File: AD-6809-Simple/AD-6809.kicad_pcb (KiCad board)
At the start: 2 copper layers, 100 x 100 mm, 41 parts, among them J1 SERIAL, J2 GAMECLK, J3 BARREL_JACK, J4 BAUD, J5 NMI, J6 RESET, SW1 RESET, U1 28C64, U2 6809, U3 28C64/IMS1630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

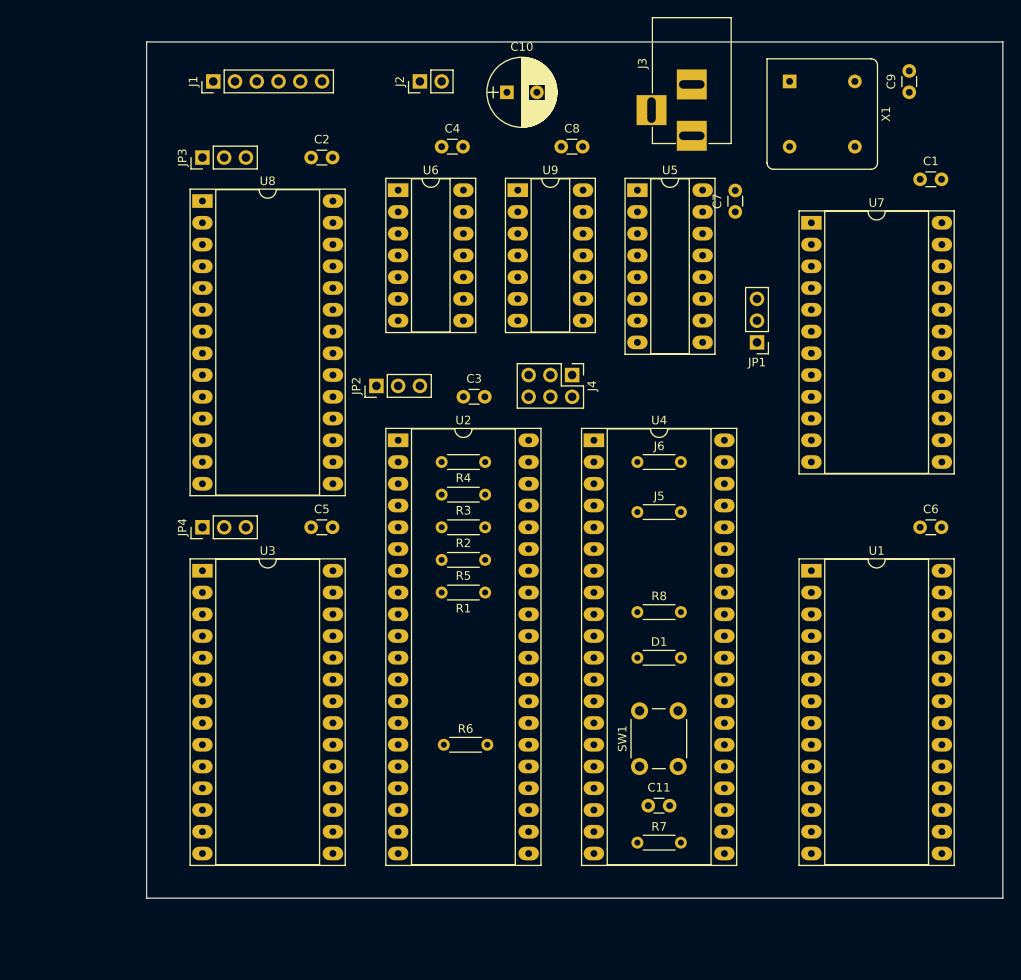
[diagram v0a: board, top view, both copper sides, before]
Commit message: Padded out the test programs to be rom sized.
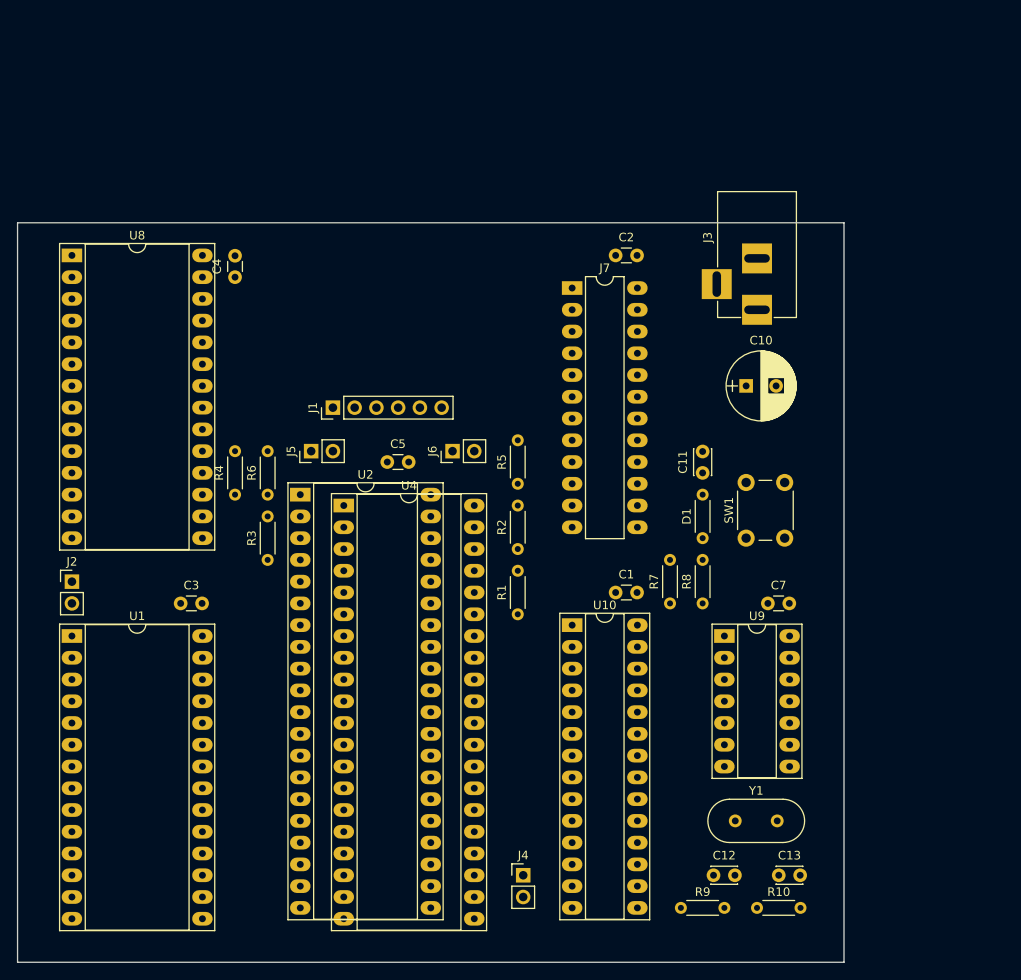
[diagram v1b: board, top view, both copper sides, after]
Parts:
- removed C6, C8, C9: 0.1uF, Capacitors_ThroughHole:C_Disc_D3.0mm_W1.6mm_P2.50mm
- removed JP1: Disable, Socket_Strips:Socket_Strip_Straight_1x03_Pitch2.54mm
- removed JP2: CLKSRC, Socket_Strips:Socket_Strip_Straight_1x03_Pitch2.54mm
- removed JP3, JP4: ROM RAM, Socket_Strips:Socket_Strip_Straight_1x03_Pitch2.54mm
- removed U3: 28C64/IMS1630, Housings_DIP:DIP-28_W15.24mm_Socket_LongPads
- removed U5: 74LS139, Housings_DIP:DIP-16_W7.62mm_Socket_LongPads
- removed U6: 74LS00, Housings_DIP:DIP-14_W7.62mm_Socket_LongPads
- removed U7: MC6850, Housings_DIP:DIP-24_W15.24mm_Socket_LongPads
- removed X1: 12.288MHz, Oscillators:Oscillator_DIP-8
- added C12: 22pF, Capacitors_ThroughHole:C_Disc_D3.0mm_W2.0mm_P2.50mm, F.Cu at (156.2, 147.3)
- added C13: 22pF, Capacitors_ThroughHole:C_Disc_D3.0mm_W2.0mm_P2.50mm, F.Cu at (163.8, 147.3)
- added J7: PAL24, Housings_DIP:DIP-24_W7.62mm_LongPads, F.Cu at (139.7, 78.7)
- added R10: 1K0, Resistors_ThroughHole:R_Axial_DIN0204_L3.6mm_D1.6mm_P5.08mm_Horizontal, F.Cu at (161.3, 151.1)
- added R9: 1M0, Resistors_ThroughHole:R_Axial_DIN0204_L3.6mm_D1.6mm_P5.08mm_Horizontal, F.Cu at (152.4, 151.1)
- added U10: SCN2661C, Housings_DIP:DIP-28_W7.62mm_Socket_LongPads, F.Cu at (139.7, 118.1)
- added Y1: 5.0688MHz, Crystals:Crystal_HC18-U_Vertical, F.Cu at (158.8, 141.0)
- C11: footprint Capacitors_ThroughHole:C_Disc_D3.0mm_W1.6mm_P2.50mm -> Capacitors_ThroughHole:C_Disc_D3.0mm_W2.0mm_P2.50mm
- J4: value BAUD -> IRQ; footprint Pin_Headers:Pin_Header_Straight_2x03_Pitch2.54mm -> Socket_Strips:Socket_Strip_Straight_1x02_Pitch2.54mm
- J5, J6: footprint Resistors_ThroughHole:R_Axial_DIN0204_L3.6mm_D1.6mm_P5.08mm_Horizontal -> Socket_Strips:Socket_Strip_Straight_1x02_Pitch2.54mm
- U8: value 28C64/IMS1630 -> IMS1630
- U9: value 74LS93 -> 74LS04
- moved U1 86.7 mm to (81.3, 119.4)
- moved J2 71.2 mm to (81.3, 113.0), turned to 0 degrees
- moved C1 59.9 mm to (144.8, 114.3)
- moved J4 58.7 mm to (134.0, 147.3), turned to 0 degrees
- moved U9 57.4 mm to (157.5, 119.4)
- moved C7 45.9 mm to (162.6, 115.6), turned to 0 degrees
- moved C10 44.2 mm to (160.0, 90.2)
- moved C3 40.9 mm to (94.0, 115.6)
- moved J1 40.6 mm to (111.8, 92.7)
- moved C11 39.4 mm to (154.9, 100.3), turned to 90 degrees
- moved J5 38.8 mm to (109.2, 97.8), turned to 90 degrees
- moved C2 37.4 mm to (144.8, 74.9)
- moved R6 35.7 mm to (104.1, 102.9), turned to 90 degrees
- moved U4 30.2 mm to (113.0, 104.1)
- moved R4 29.5 mm to (100.3, 102.9), turned to 90 degrees
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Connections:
- net /PHI2 renamed /E
- J1 pad 1: Net-(J1-Pad1) -> (no net)
- J1 pad 4: Net-(J1-Pad4) -> (no net)
- J1 pad 5: Net-(J1-Pad5) -> /DTR
- J4 pad 1: Net-(J4-Pad1) -> /~IRQ
- J4 pad 2: /SERCLK -> Net-(J4-Pad2)
- U1 pad 1: Net-(U1-Pad1) -> (no net)
- U1 pad 20: /~MEM3 -> /~ROM_SEL
- U1 pad 26: Net-(U1-Pad26) -> (no net)
- U2 pad 35: Net-(U2-Pad35) -> (no net)
- U2 pad 38: Net-(JP2-Pad2) -> Net-(J2-Pad2)
- U2 pad 5: Net-(U2-Pad5) -> (no net)
- U2 pad 6: Net-(U2-Pad6) -> (no net)
- U4 pad 2: Net-(U4-Pad2) -> (no net)
- U4 pad 3: Net-(U4-Pad3) -> (no net)
- U4 pad 35: Net-(U4-Pad35) -> (no net)
- U4 pad 36: Net-(U4-Pad36) -> (no net)
- U4 pad 37: Net-(U4-Pad37) -> (no net)
- U4 pad 38: Net-(U4-Pad38) -> (no net)
- U4 pad 4: Net-(U4-Pad4) -> (no net)
- U4 pad 5: Net-(U4-Pad5) -> (no net)
- U4 pad 7: Net-(U4-Pad7) -> (no net)
- U8 pad 1: Net-(U8-Pad1) -> (no net)
- U8 pad 20: /~MEM2 -> /~RAM_SEL
- U8 pad 26: Net-(JP3-Pad2) -> +5V
- U9 pad 1: /CPUCLK -> (no net)
- U9 pad 10: GND -> (no net)
- U9 pad 11: Net-(J4-Pad5) -> (no net)
- U9 pad 12: /CPUCLK -> (no net)
- U9 pad 14: Net-(U9-Pad14) -> +5V
- U9 pad 2: GND -> (no net)
- U9 pad 3: GND -> Net-(C12-Pad1)
- U9 pad 4: (no net) -> Net-(R10-Pad1)
- U9 pad 5: +5V -> Net-(R10-Pad1)
- U9 pad 6: (no net) -> /SERCLK
- U9 pad 7: (no net) -> GND
- U9 pad 8: Net-(J4-Pad3) -> (no net)
- U9 pad 9: Net-(J4-Pad1) -> (no net)
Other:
- board size 100 x 100 mm -> 96.5 x 86.4 mm
- net class Power removed
- rule pad_to_mask_clearance: 0.2 -> 0
